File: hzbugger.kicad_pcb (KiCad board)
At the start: 2 copper layers, 53.5 x 26.7 mm, 56 parts, among them J2 IDC, J4 SWD, J6 GPIO, SW1 RESET_SW, SW2 BOOT0_SW, U1 STM32F103C8T6, U2 SRV05-4, U3 AMS1117-3.3, U4 HX AM 90D, Y1 8M

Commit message: final adjustments
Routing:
- net GND: vias 163 -> 164
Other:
- board text added: "PA4"
- board text removed: "A4"
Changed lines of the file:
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@@
 	(gr_text "HZBUGGER"
 		(at 137.4 77.8 0)
-		(layer "F.SilkS")
+		(layer "F.SilkS" knockout)
 		(effects
 			(font
-				(face "DejaVu Sans Condensed")
-				(size 2.4 1.5)
-				(thickness 0.25)
+				(size 2.2 1.5)
+				(thickness 0.375)
 				(bold yes)
 			)
 			(justify left bottom)
-		)
-		(render_cache "HZBUGGER" 0
-			(polygon
-				(pts
-					(xy 137.573198 74.944247) (xy 137.928755 74.944247) (xy 137.928755 75.877157) (xy 138.452381 75.877157)
-					(xy 138.452381 74.944247) (xy 138.806838 74.944247) (xy 138.806838 77.392) (xy 138.452381 77.392)
-					(xy 138.452381 76.354163) (xy 137.928755 76.354163) (xy 137.928755 77.392) (xy 137.573198 77.392)
-				)
-			)
-			(polygon
-				(pts
-					(xy 139.086374 74.944247) (xy 140.243169 74.944247) (xy 140.243169 75.326291) (xy 139.504396 76.914847)
-					(xy 140.264693 76.914847) (xy 140.264693 77.392) (xy 139.06485 77.392) (xy 139.06485 77.009955)
-					(xy 139.803624 75.421399) (xy 139.086374 75.421399)
-				)
-			)
-			(polygon
-				(pts
-					(xy 141.203112 74.956395) (xy 141.317749 74.989009) (xy 141.404877 75.037375) (xy 141.470032 75.098413)
-					(xy 141.52427 75.182857) (xy 141.56402 75.289587) (xy 141.589428 75.423552) (xy 141.598626 75.591832)
-					(xy 141.593057 75.709046) (xy 141.577249 75.809502) (xy 141.552006 75.896061) (xy 141.516415 75.971844)
-					(xy 141.471256 76.033543) (xy 141.415169 76.082027) (xy 141.48645 76.133059) (xy 141.544944 76.205192)
-					(xy 141.592397 76.300087) (xy 141.626253 76.410211) (xy 141.647465 76.53896) (xy 141.654954 76.690339)
-					(xy 141.645462 76.865589) (xy 141.619024 77.007946) (xy 141.577344 77.123942) (xy 141.520224 77.218196)
-					(xy 141.451162 77.2887) (xy 141.362949 77.343055) (xy 141.251254 77.378875) (xy 141.110903 77.392)
-					(xy 140.521698 77.392) (xy 140.521698 76.962474) (xy 140.877254 76.962474) (xy 141.085258 76.962474)
-					(xy 141.155323 76.95221) (xy 141.207732 76.924554) (xy 141.246641 76.882167) (xy 141.275301 76.823011)
-					(xy 141.293656 76.744179) (xy 141.300405 76.639487) (xy 141.293687 76.537016) (xy 141.275365 76.459526)
-					(xy 141.246641 76.401057) (xy 141.20777 76.359087) (xy 141.155363 76.331666) (xy 141.085258 76.321483)
-					(xy 140.877254 76.321483) (xy 140.877254 76.962474) (xy 140.521698 76.962474) (xy 140.521698 75.891811)
-					(xy 140.877254 75.891811) (xy 141.072984 75.891811) (xy 141.127526 75.883552) (xy 141.169023 75.861099)
-					(xy 141.200479 75.826305) (xy 141.223834 75.778165) (xy 141.238664 75.715201) (xy 141.244077 75.632865)
-					(xy 141.238697 75.551511) (xy 141.223892 75.48871) (xy 141.200479 75.440157) (xy 141.168978 75.40486)
-					(xy 141.127479 75.382126) (xy 141.072984 75.373772) (xy 140.877254 75.373772) (xy 140.877254 75.891811)
-					(xy 140.521698 75.891811) (xy 140.521698 74.944247) (xy 141.054483 74.944247)
-				)
-			)
-			(polygon
-				(pts
-					(xy 141.960777 74.944247) (xy 142.316333 74.944247) (xy 142.316333 76.411609) (xy 142.324107 76.613986)
-					(xy 142.344 76.753048) (xy 142.372112 76.845237) (xy 142.415324 76.91558) (xy 142.474177 76.959463)
-					(xy 142.554012 76.975517) (xy 142.634589 76.959411) (xy 142.693731 76.915482) (xy 142.736919 76.845237)
-					(xy 142.765081 76.753036) (xy 142.785004 76.613973) (xy 142.79279 76.411609) (xy 142.79279 74.944247)
-					(xy 143.148346 74.944247) (xy 143.148346 76.411609) (xy 143.141264 76.626874) (xy 143.121526 76.806978)
-					(xy 143.090954 76.95719) (xy 143.050713 77.082081) (xy 143.001251 77.18537) (xy 142.940186 77.272375)
-					(xy 142.867171 77.341977) (xy 142.780256 77.394167) (xy 142.676884 77.427559) (xy 142.554012 77.43948)
-					(xy 142.431121 77.42755) (xy 142.3278 77.394144) (xy 142.24099 77.341947) (xy 142.16812 77.272352)
-					(xy 142.107231 77.18537) (xy 142.058008 77.082141) (xy 142.017944 76.957286) (xy 141.987495 76.807077)
-					(xy 141.967833 76.626941) (xy 141.960777 76.411609)
-				)
-			)
-			(polygon
-				(pts
-					(xy 144.731407 77.20999) (xy 144.595357 77.310676) (xy 144.455259 77.382181) (xy 144.310696 77.425055)
-					(xy 144.160703 77.43948) (xy 144.022833 77.424502) (xy 143.901682 77.381633) (xy 143.794706 77.312858)
-					(xy 143.699829 77.218606) (xy 143.615553 77.097736) (xy 143.545431 76.956528) (xy 143.490073 76.796312)
-					(xy 143.449276 76.614364) (xy 143.423672 76.407163) (xy 143.414693 76.170541) (xy 143.423864 75.931195)
-					(xy 143.449973 75.72244) (xy 143.491513 75.539878) (xy 143.547824 75.379809) (xy 143.619125 75.23939)
-					(xy 143.704515 75.120073) (xy 143.801385 75.026544) (xy 143.91138 74.95796) (xy 144.036725 74.915033)
-					(xy 144.18012 74.89999) (xy 144.315562 74.911625) (xy 144.443444 74.945859) (xy 144.566423 75.003101)
-					(xy 144.681215 75.082) (xy 144.681215 75.588608) (xy 144.563977 75.485417) (xy 144.451687 75.414805)
-					(xy 144.337147 75.371587) (xy 144.223168 75.357359) (xy 144.118527 75.371875) (xy 144.03121 75.412777)
-					(xy 143.957913 75.477993) (xy 143.896279 75.568092) (xy 143.84858 75.677361) (xy 143.81281 75.810715)
-					(xy 143.789798 75.973078) (xy 143.781516 76.170541) (xy 143.789507 76.366639) (xy 143.811719 76.528286)
-					(xy 143.846227 76.661356) (xy 143.892158 76.770646) (xy 143.951959 76.861512) (xy 144.022702 76.926875)
-					(xy 144.106584 76.967673) (xy 144.206773 76.982111) (xy 144.309721 76.969801) (xy 144.355709 76.953567)
-					(xy 144.394351 76.93126) (xy 144.394351 76.455866) (xy 144.178105 76.455866) (xy 144.178105 76.032935)
-					(xy 144.731407 76.032935)
-				)
-			)
-			(polygon
-				(pts
-					(xy 146.280395 77.20999) (xy 146.144345 77.310676) (xy 146.004248 77.382181) (xy 145.859684 77.425055)
-					(xy 145.709691 77.43948) (xy 145.571821 77.424502) (xy 145.45067 77.381633) (xy 145.343694 77.312858)
-					(xy 145.248817 77.218606) (xy 145.164541 77.097736) (xy 145.09442 76.956528) (xy 145.039061 76.796312)
-					(xy 144.998265 76.614364) (xy 144.972661 76.407163) (xy 144.963681 76.170541) (xy 144.972852 75.931195)
-					(xy 144.998961 75.72244) (xy 145.040501 75.539878) (xy 145.096812 75.379809) (xy 145.168113 75.23939)
-					(xy 145.253503 75.120073) (xy 145.350373 75.026544) (xy 145.460369 74.95796) (xy 145.585713 74.915033)
-					(xy 145.729108 74.89999) (xy 145.86455 74.911625) (xy 145.992432 74.945859) (xy 146.115411 75.003101)
-					(xy 146.230203 75.082) (xy 146.230203 75.588608) (xy 146.112965 75.485417) (xy 146.000676 75.414805)
-					(xy 145.886135 75.371587) (xy 145.772156 75.357359) (xy 145.667515 75.371875) (xy 145.580198 75.412777)
-					(xy 145.506901 75.477993) (xy 145.445267 75.568092) (xy 145.397568 75.677361) (xy 145.361798 75.810715)
-					(xy 145.338786 75.973078) (xy 145.330504 76.170541) (xy 145.338495 76.366639) (xy 145.360707 76.528286)
-					(xy 145.395215 76.661356) (xy 145.441146 76.770646) (xy 145.500947 76.861512) (xy 145.57169 76.926875)
-					(xy 145.655573 76.967673) (xy 145.755761 76.982111) (xy 145.858709 76.969801) (xy 145.904697 76.953567)
-					(xy 145.94334 76.93126) (xy 145.94334 76.455866) (xy 145.727093 76.455866) (xy 145.727093 76.032935)
-					(xy 146.280395 76.032935)
-				)
-			)
-			(polygon
-				(pts
-					(xy 146.591621 74.944247) (xy 147.549664 74.944247) (xy 147.549664 75.421399) (xy 146.947178 75.421399)
-					(xy 146.947178 75.877157) (xy 147.51376 75.877157) (xy 147.51376 76.354163) (xy 146.947178 76.354163)
-					(xy 146.947178 76.914847) (xy 147.57018 76.914847) (xy 147.57018 77.392) (xy 146.591621 77.392)
-				)
-			)
-			(polygon
-				(pts
-					(xy 148.563424 74.956776) (xy 148.67298 74.990668) (xy 148.757669 75.041505) (xy 148.822322 75.106619)
-					(xy 148.875447 75.194617) (xy 148.914641 75.305685) (xy 148.939788 75.444988) (xy 148.9489 75.619676)
-					(xy 148.940912 75.778493) (xy 148.918566 75.90958) (xy 148.883321 76.018133) (xy 148.833674 76.110545)
-					(xy 148.768401 76.187006) (xy 148.684569 76.247624) (xy 148.730417 76.27478) (xy 148.773748 76.318622)
-					(xy 148.815177 76.381274) (xy 148.869306 76.501731) (xy 148.931498 76.696787) (xy 149.124114 77.392)
-					(xy 148.746026 77.392) (xy 148.578964 76.783688) (xy 148.523159 76.618908) (xy 148.475466 76.532949)
-					(xy 148.438524 76.496744) (xy 148.393148 76.473882) (xy 148.337164 76.465684) (xy 148.23678 76.465684)
-					(xy 148.23678 77.392) (xy 147.881223 77.392) (xy 147.881223 76.029564) (xy 148.23678 76.029564)
-					(xy 148.386348 76.029564) (xy 148.458867 76.01974) (xy 148.510135 75.994) (xy 148.545625 75.955852)
-					(xy 148.571057 75.901226) (xy 148.587951 75.823066) (xy 148.594351 75.713172) (xy 148.587944 75.604411)
-					(xy 148.571052 75.527401) (xy 148.545625 75.473863) (xy 148.510217 75.436534) (xy 148.458957 75.411271)
-					(xy 148.386348 75.401616) (xy 148.23678 75.401616) (xy 148.23678 76.029564) (xy 147.881223 76.029564)
-					(xy 147.881223 74.944247) (xy 148.423259 74.944247)
-				)
-			)
 		)
 	)
@@
 		)
 	)
-	(gr_text "A4"
+	(gr_text "PA4"
 		(at 136.8 80 0)
 		(layer "F.SilkS")
@@
 	)
 	(via
-		(at 111.308119 98.616398)
+		(at 112.8 99)
 		(size 0.6)
 		(drill 0.3)
@@
 	)
 	(via
-		(at 138.6 77.8)
+		(at 137.2 77)
 		(size 0.6)
 		(drill 0.3)
@@
 		(size 0.6)
 		(drill 0.3)
+		(layers "F.Cu" "B.Cu")
+		(free yes)
+		(net 9)
+	)
+	(via
+		(at 110.8 98.6)
+		(size 0.6)
+		(drill 0.3)

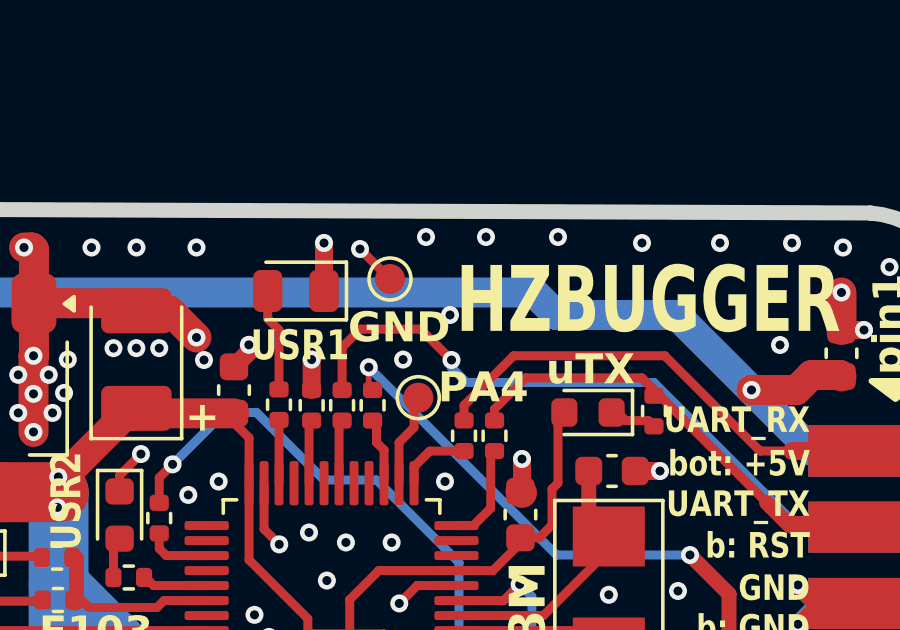
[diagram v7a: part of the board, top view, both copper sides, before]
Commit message: one via in wrong place
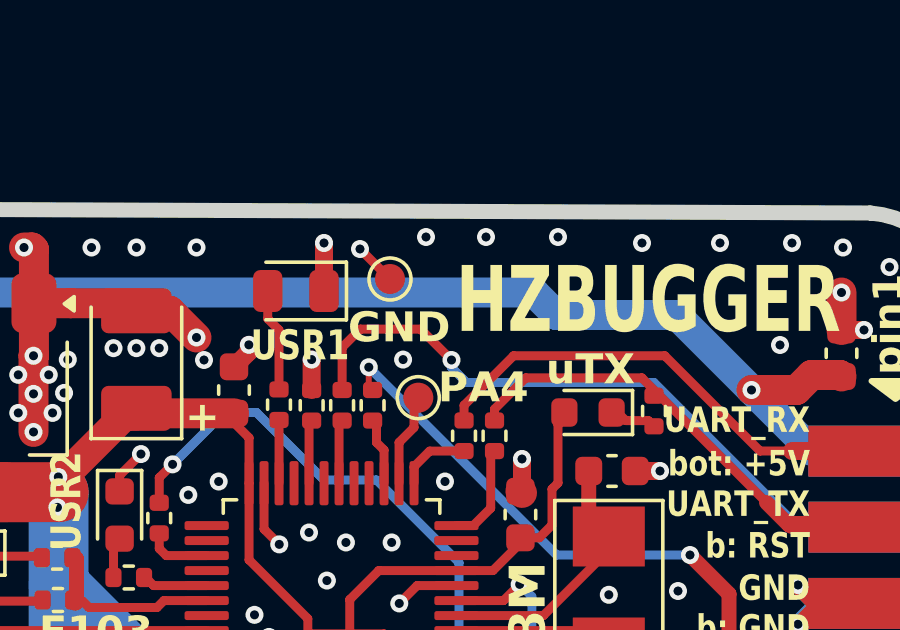
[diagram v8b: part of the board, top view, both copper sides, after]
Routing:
- net GND: vias 164 -> 163
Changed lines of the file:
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@@
-	)
-	(via
-		(at 137.2 77)
-		(size 0.6)
-		(drill 0.3)
-		(layers "F.Cu" "B.Cu")
-		(free yes)
-		(net 9)
 	)
 	(via
